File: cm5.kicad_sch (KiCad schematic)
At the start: 0 parts

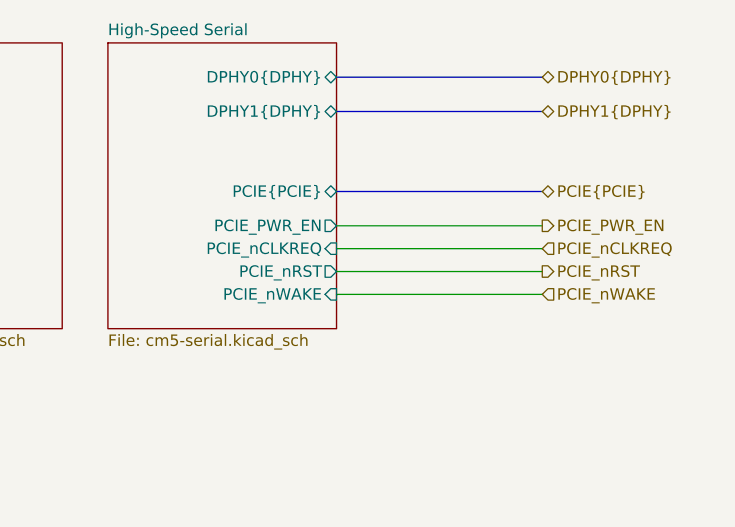
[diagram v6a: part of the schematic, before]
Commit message: abstractified pcie sideband sigs
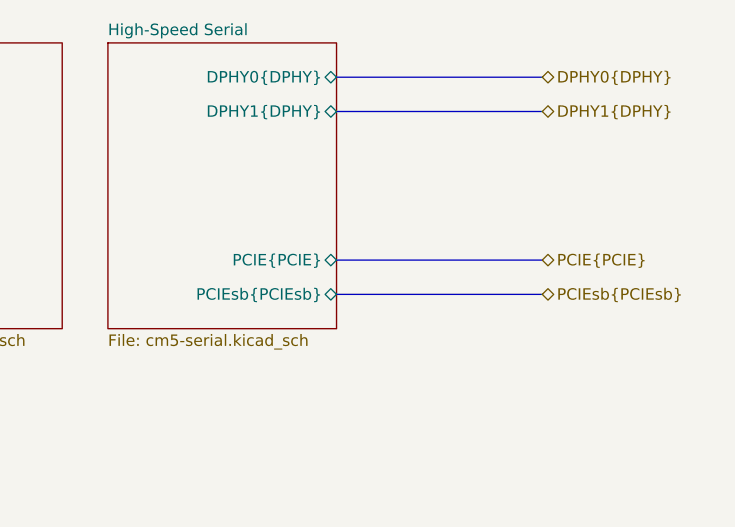
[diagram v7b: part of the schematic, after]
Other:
- sheet High-Speed Serial ports: added PCIEsb{PCIEsb}; removed PCIE_PWR_EN, PCIE_nCLKREQ, PCIE_nRST, PCIE_nWAKE
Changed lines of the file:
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@@
+		)
+	)
+	(bus
+		(pts
+			(xy 100.33 96.52) (xy 123.19 96.52)
+		)
+		(stroke
+			(width 0)
+			(type default)
+		)
+	)
+	(bus
+		(pts
+			(xy 179.07 104.14) (xy 201.93 104.14)
+		)
+		(stroke
+			(width 0)
+			(type default)
+		)
+	)
+	(bus
+		(pts
+			(xy 179.07 100.33) (xy 201.93 100.33)
+		)
+		(stroke
+			(width 0)
+			(type default)
+		)
+	)
+	(bus
+		(pts
+			(xy 100.33 88.9) (xy 123.19 88.9)
+		)
+		(stroke
+			(width 0)
+			(type default)
+		)
+	)
+	(bus
+		(pts
+			(xy 179.07 80.01) (xy 201.93 80.01)
+		)
+		(stroke
+			(width 0)
+			(type default)
 		)
 	)
 	(wire
 		(pts
-			(xy 179.07 104.14) (xy 201.93 104.14)
-		)
-		(stroke
-			(width 0)
-			(type default)
-		)
-	)
-	(bus
-		(pts
-			(xy 100.33 96.52) (xy 123.19 96.52)
-		)
-		(stroke
-			(width 0)
-			(type default)
+			(xy 100.33 83.82) (xy 123.19 83.82)
+		)
+		(stroke
+			(width 0.381)
+			(type default)
+			(color 255 153 0 1)
 		)
 	)
 	(wire
 		(pts
-			(xy 179.07 99.06) (xy 201.93 99.06)
-		)
-		(stroke
-			(width 0)
-			(type default)
-		)
-	)
-	(bus
-		(pts
-			(xy 179.07 92.71) (xy 201.93 92.71)
-		)
-		(stroke
-			(width 0)
-			(type default)
-		)
-	)
-	(bus
-		(pts
-			(xy 100.33 88.9) (xy 123.19 88.9)
-		)
-		(stroke
-			(width 0)
-			(type default)
-		)
-	)
-	(bus
-		(pts
-			(xy 179.07 80.01) (xy 201.93 80.01)
-		)
-		(stroke
-			(width 0)
-			(type default)
+			(xy 100.33 80.01) (xy 123.19 80.01)
+		)
+		(stroke
+			(width 0.508)
+			(type default)
+			(color 255 0 0 1)
 		)
 	)
 	(wire
 		(pts
-			(xy 100.33 83.82) (xy 123.19 83.82)
-		)
-		(stroke
-			(width 0.381)
-			(type default)
-			(color 255 153 0 1)
+			(xy 100.33 104.14) (xy 123.19 104.14)
+		)
+		(stroke
+			(width 0)
+			(type default)
+		)
+	)
+	(bus
+		(pts
+			(xy 100.33 92.71) (xy 123.19 92.71)
+		)
+		(stroke
+			(width 0)
+			(type default)
+		)
+	)
+	(bus
+		(pts
+			(xy 179.07 83.82) (xy 201.93 83.82)
+		)
+		(stroke
+			(width 0)
+			(type default)
 		)
 	)
 	(wire
 		(pts
-			(xy 179.07 101.6) (xy 201.93 101.6)
-		)
-		(stroke
-			(width 0)
-			(type default)
-		)
-	)
-	(wire
-		(pts
-			(xy 100.33 80.01) (xy 123.19 80.01)
-		)
-		(stroke
-			(width 0.508)
-			(type default)
-			(color 255 0 0 1)
-		)
-	)
-	(wire
-		(pts
-			(xy 100.33 104.14) (xy 123.19 104.14)
-		)
-		(stroke
-			(width 0)
-			(type default)
-		)
-	)
-	(bus
-		(pts
-			(xy 100.33 92.71) (xy 123.19 92.71)
-		)
-		(stroke
-			(width 0)
-			(type default)
-		)
-	)
-	(bus
-		(pts
-			(xy 179.07 83.82) (xy 201.93 83.82)
-		)
-		(stroke
-			(width 0)
-			(type default)
-		)
-	)
-	(wire
-		(pts
 			(xy 100.33 101.6) (xy 123.19 101.6)
 		)
@@
 			(width 0)
 			(type default)
-		)
-	)
-	(wire
-		(pts
-			(xy 179.07 96.52) (xy 201.93 96.52)
-		)
-		(stroke
-			(width 0)
-			(type default)
-		)
-	)
-	(hierarchical_label "PCIE_PWR_EN"
-		(shape output)
-		(at 201.93 96.52 0)
-		(effects
-			(font
-				(size 1.27 1.27)
-			)
-			(justify left)
-		)
-	)
-	(hierarchical_label "PCIE_nWAKE"
-		(shape input)
-		(at 201.93 104.14 0)
-		(effects
-			(font
-				(size 1.27 1.27)
-			)
-			(justify left)
 		)
 	)
@@
 		)
 	)
-	(hierarchical_label "PCIE_nCLKREQ"
-		(shape input)
-		(at 201.93 99.06 0)
-		(effects
-			(font
-				(size 1.27 1.27)
-			)
-			(justify left)
-		)
-	)
 	(hierarchical_label "CAM_GPIO1"
 		(shape output)
@@
 		)
 	)
-	(hierarchical_label "PCIE_nRST"
-		(shape output)
-		(at 201.93 101.6 0)
+	(hierarchical_label "DPHY1{DPHY}"
+		(shape bidirectional)
+		(at 201.93 83.82 0)
 		(effects
 			(font
@@
 		)
 	)
-	(hierarchical_label "DPHY1{DPHY}"
-		(shape bidirectional)
-		(at 201.93 83.82 0)
+	(hierarchical_label "SPI0{SPI}"
+		(shape bidirectional)
+		(at 100.33 96.52 180)
+		(effects
+			(font
+				(size 1.27 1.27)
+			)
+			(justify right)
+		)
+	)
+	(hierarchical_label "PCIE{PCIE}"
+		(shape bidirectional)
+		(at 201.93 100.33 0)
 		(effects
 			(font
@@
 		)
 	)
-	(hierarchical_label "SPI0{SPI}"
-		(shape bidirectional)
-		(at 100.33 96.52 180)
-		(effects
-			(font
-				(size 1.27 1.27)
-			)
-			(justify right)
-		)
-	)
-	(hierarchical_label "PCIE{PCIE}"
-		(shape bidirectional)
-		(at 201.93 92.71 0)
+	(hierarchical_label "PCIEsb{PCIEsb}"
+		(shape bidirectional)
+		(at 201.93 104.14 0)
 		(effects
 			(font
@@
 			)
 		)
-		(pin "PCIE_nCLKREQ" input
-			(at 179.07 99.06 0)
+		(pin "PCIE{PCIE}" bidirectional
+			(at 179.07 100.33 0)
 			(effects
 				(font
@@
 			)
 		)
-		(pin "PCIE_nRST" output
-			(at 179.07 101.6 0)
-			(effects
-				(font
-					(size 1.27 1.27)
-				)
-				(justify right)
-			)
-		)
-		(pin "PCIE_nWAKE" input
+		(pin "PCIEsb{PCIEsb}" bidirectional
 			(at 179.07 104.14 0)
 			(effects
 				(font
-					(size 1.27 1.27)
-				)
-				(justify right)
-			)
-		)
-		(pin "PCIE_PWR_EN" output
-			(at 179.07 96.52 0)
-			(effects
-				(font
-					(size 1.27 1.27)
-				)
-				(justify right)
-			)
-		)
-		(pin "PCIE{PCIE}" bidirectional
-			(at 179.07 92.71 0)
-			(effects
-				(font

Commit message: neo m8m impl.
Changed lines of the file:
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@@
 		)
 	)
-	(hierarchical_label "SPI0{SPI}"
+	(hierarchical_label "I2C0{I2C}"
 		(shape bidirectional)
 		(at 100.33 88.9 180)
@@
 		)
 		(fill
-			(color 0 0 0 0.0000)
+			(color 0 194 0 0.1100)
 		)
 		(property "Sheetname" "GPIO"
@@
 		)
 		(fill
-			(color 0 0 0 0.0000)
+			(color 0 194 0 0.1098)
 		)
 		(property "Sheetname" "High-Speed Serial"
